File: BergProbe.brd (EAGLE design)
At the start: 100 x 47.5 mm, 16 parts, among them Q1 DMG6602SVT, Q2 DMG6602SVT, U1 DS3231SN

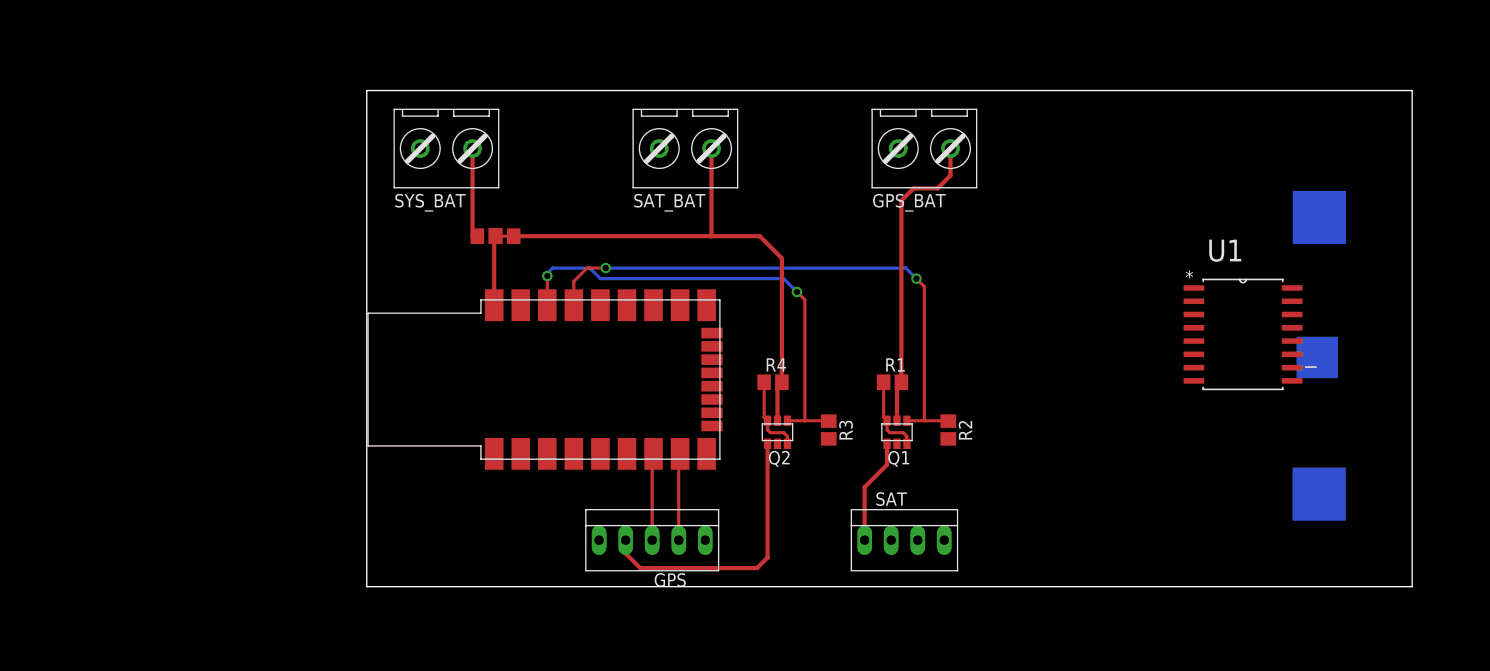
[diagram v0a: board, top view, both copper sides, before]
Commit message: Progress on PCB layout. Added analogue headers to schematic.
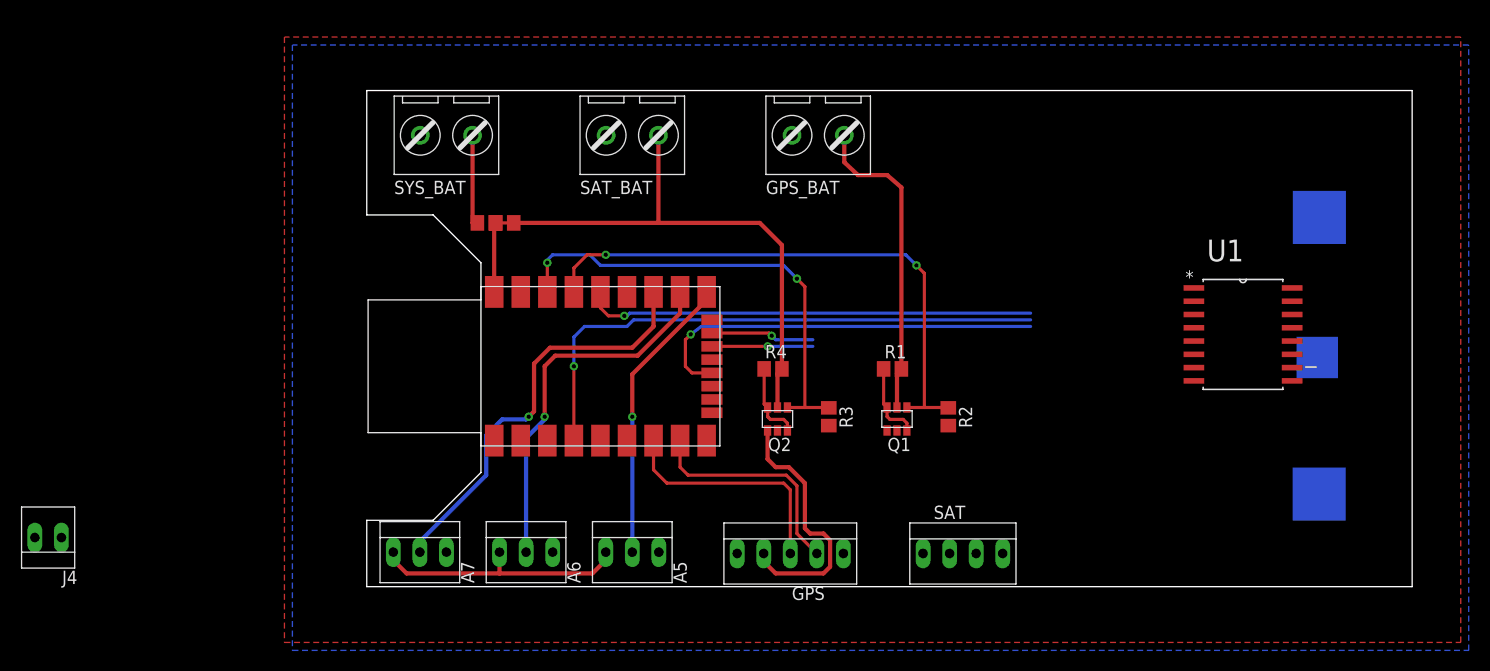
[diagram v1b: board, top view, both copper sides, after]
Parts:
- added A5, A6, A7: 3-PIN-MOLEX, farnell-parts:3-MOLEX
- added J4: 2-PIN-MOLEX, farnell-parts:2-MOLEX
- moved GPS 13.3 mm to (41.7, 3.05)
- moved GPS_BAT 10.2 mm to (43.2, 43.2)
- moved SAT 5.73 mm to (58.2, 2.79)
- moved SAT_BAT 5.24 mm to (25.4, 43.2)
- moved R500 1.27 mm to (13.2, 34.8)
- moved R600 1.27 mm to (11.4, 34.8)
- moved SYS_BAT 1.27 mm to (7.62, 43.2)
- moved Q1 1.27 mm to (52.1, 15.2)
- moved Q2 1.27 mm to (40.6, 15.2)
- moved R1 1.27 mm to (50.3, 20.8)
- moved R2 1.27 mm to (55.6, 16.3)
- moved R3 1.27 mm to (44.2, 16.3)
- moved R4 1.27 mm to (38.9, 20.8)
- moved U$1 1.27 mm to (26.2, 21.1)
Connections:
- new net ADC_A5: A5.2, U$1.A5
- new net ADC_A6: A6.2, U$1.A6
- new net ADC_A7: A7.2, U$1.A7
- net +3V3: now also A5.3, A6.3, A7.3
- net GND: now also A5.1, A6.1, A7.1
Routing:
- net I2C_SDA: track 0.00 -> 54.3 mm, vias 0 -> 1
- net I2C_SCK: track 0.00 -> 43.1 mm, vias 0 -> 1
- net ADC_A7: track 0.00 -> 40.1 mm, vias 0 -> 1
- net RTC_INT: track 0.00 -> 38.8 mm, vias 0 -> 1
- net ADC_A6: track 0.00 -> 35.6 mm, vias 0 -> 1
- net ADC_A5: track 0.00 -> 27.8 mm, vias 0 -> 1
- net +3V3: track 0.00 -> 24.9 mm
- net USART1_TX: track 8.31 -> 22.8 mm
- net USART1_RX: track 8.31 -> 21.7 mm
- net GPS_PWR: track 10.1 -> 0.00 mm
- net USART2_RX: track 0.00 -> 9.92 mm, vias 0 -> 1
- net USART2_TX: track 0.00 -> 9.65 mm, vias 0 -> 1
- net SAT_PWR: track 26.7 -> 24.8 mm
- net GPS_BAT: track 29.5 -> 30.2 mm
- added copper zone on layer 1, net GND
- added copper zone on layer 16, net GND
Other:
- outline, holes or cut-outs redrawn

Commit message: PCB Layout complete EXCEPT for wakeup switch/RTC Alarm finalisation.
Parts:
- removed J4: 2-PIN-MOLEX, farnell-parts:2-MOLEX
- added WAKE: 2-PIN-MOLEX, farnell-parts:2-MOLEX
- moved U$2 30.2 mm to (52.1, 23.6)
- moved U1 25.6 mm to (61.2, 36.1), turned to 90 degrees
- moved SAT 2.54 mm to (55.6, 2.79)
- moved R2 1.02 mm to (54.6, 16.3)
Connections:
- new net A1: U$1.A1
- new net A10: U$1.A10
- new net A4: U$1.A4
- new net A8: U$1.A8
- new net B1: U$1.B1
- new net B15: U$1.B15
- new net B4: U$1.B4
- new net B5: U$1.B5
- new net B8: U$1.B8
- new net B9: U$1.B9
- new net N$1: WAKE.1
- new net N$3: WAKE.2
- net GPS_PWR: now also GPS.4; no longer SAT.4
- net SAT_PWR: now also SAT.4; no longer GPS.4
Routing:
- net +3V3: track 24.9 -> 107.7 mm, vias 0 -> 3
- net USART2_RX: track 9.92 -> 40.4 mm, vias 1 -> 2
- net USART2_TX: track 9.65 -> 37.2 mm, vias 1 -> 2
- net B15: track 0.00 -> 27.4 mm, vias 0 -> 1
- net GPS_PWR: track 0.00 -> 22.8 mm, vias 0 -> 1
- net B1: track 0.00 -> 14.9 mm, vias 0 -> 1
- net B4: track 0.00 -> 8.76 mm, vias 0 -> 1
- net B5: track 0.00 -> 7.74 mm, vias 0 -> 1
- net I2C_SDA: track 54.3 -> 61.9 mm, vias 1 -> 2
- net I2C_SCK: track 43.1 -> 49.4 mm, vias 1 -> 2
- net RTC_BAT: track 0.00 -> 6.10 mm, vias 0 -> 1
- net RTC_INT: track 38.8 -> 43.4 mm, vias 1 -> 2
- net A8: track 0.00 -> 3.52 mm, vias 0 -> 1
- net B8: track 0.00 -> 3.27 mm, vias 0 -> 1
- net SAT_PWR: track 24.8 -> 21.8 mm
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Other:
- board size 100 x 47.5 mm -> 70 x 47.5 mm
- board text added: "Bergprobe V1.0"
- board text added: "Espruino Pico"
- board text added: "Graeme Bragg, Kirk Martinez"
- board text added: "University of Southampton"
- board text added: "http://glacsweb.org"

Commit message: FInal PCB and schematic version
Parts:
- added Q3: DMG6602SVT, farnell-parts:TSOT26
- added R5, R6: 100K, resistor:R0805
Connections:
- removed net N$1: WAKE.1
- removed net N$3: WAKE.2
- new net WAKE: Q3.P$4, R6.2, U$1.A0
- net +3V3: now also Q3.P$2, R5.2
- net GND: now also Q3.P$1, Q3.P$5, Q3.P$6, R6.1, WAKE.1
- net RTC_INT: now also Q3.P$3, R5.1, WAKE.2; no longer U$1.A0
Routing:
- net WAKE: track 0.00 -> 23.0 mm, vias 0 -> 2
- net RTC_INT: track 43.4 -> 56.1 mm, vias 2 -> 3
- net +3V3: track 107.7 -> 113.9 mm, vias 3 -> 4
- net GPS_EN: track 54.8 -> 52.9 mm
